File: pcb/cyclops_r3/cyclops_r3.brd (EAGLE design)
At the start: 69.8 x 53.3 mm, 111 parts, among them M12_TUBE_MOUNT PT-LH001, Q1 SUM11006, Q2 IRF540, U1 MCP4921, U10 AD829, U11 MIC5225, U12 MIC5270, U2 317-N, U3 TLV37, U4 337-N, U5 ADR03, U6 OP1177, U7 TLV2374, U8 ZXTD45, U9 ADA4899

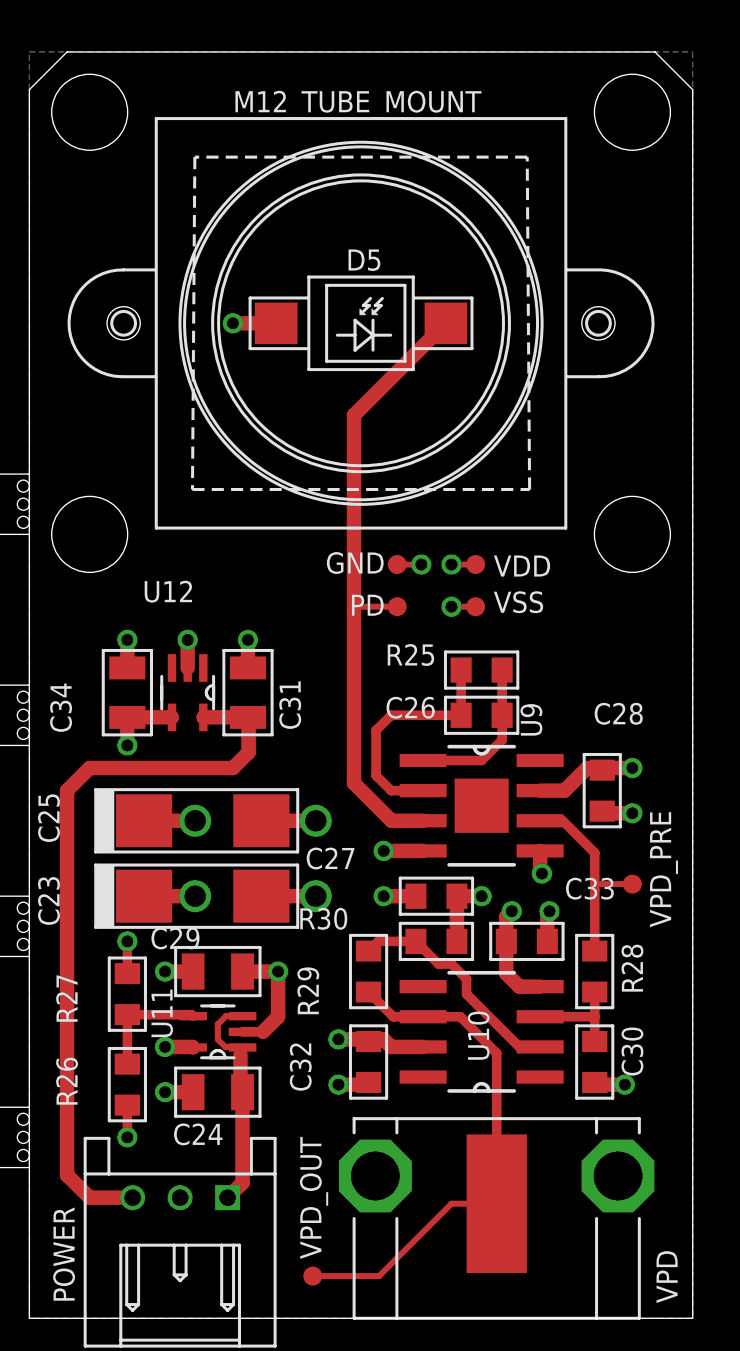
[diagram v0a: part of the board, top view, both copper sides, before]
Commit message: Added a compensation cap and offset null pot to the PD circuit.
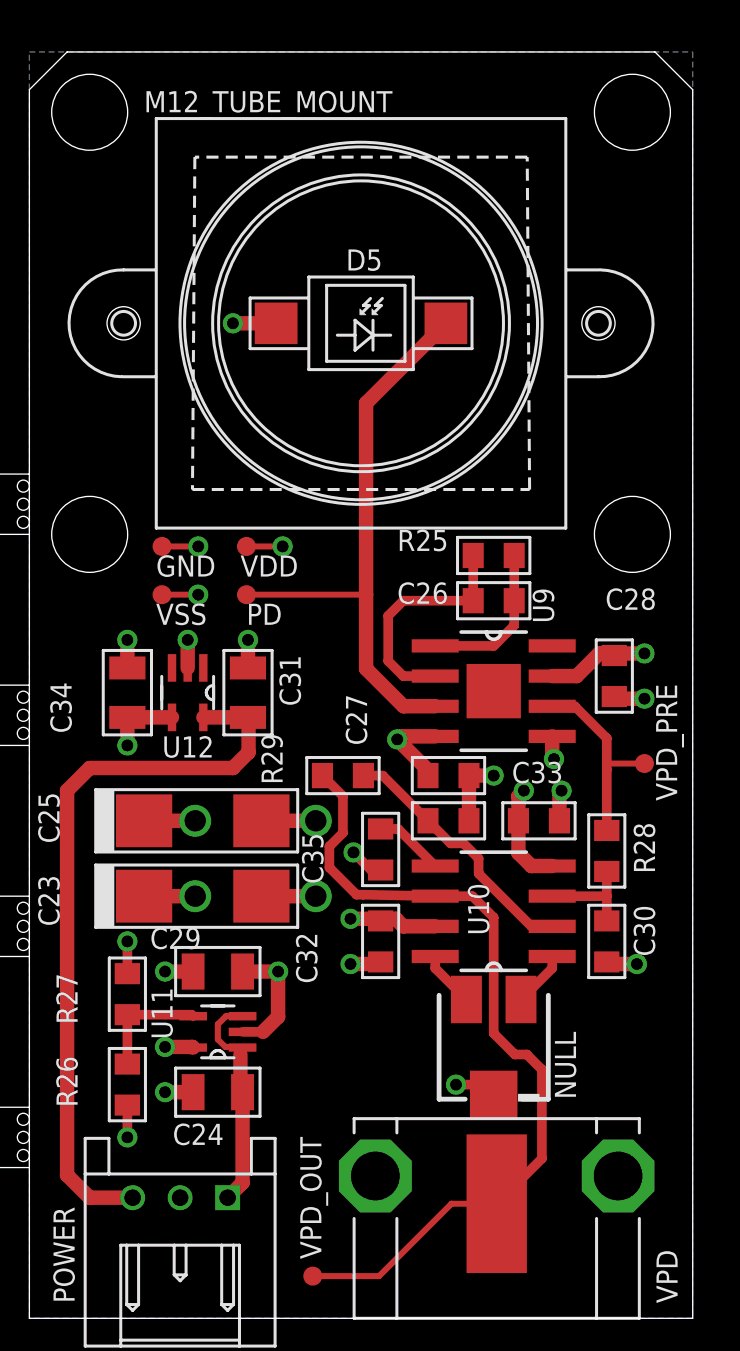
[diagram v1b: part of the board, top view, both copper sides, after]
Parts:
- added C35: 10pF, cyclops:0603
- added NULL: 20k, cyclops:SM-42/43A
- moved VSS 13.2 mm to (76.7, 30.5)
- moved GND 9.94 mm to (76.7, 32.5)
- moved VDD 9.68 mm to (80.3, 32.5)
- moved R29 8.33 mm to (84.3, 22.9), turned to 0 degrees
- moved PD 6.37 mm to (80.3, 30.5)
- moved C30 5.11 mm to (95.4, 15.9)
- moved C32 5.11 mm to (85.9, 15.9)
- moved U10 5.11 mm to (90.7, 17.1)
- moved VPD_PRE 5.11 mm to (97.0, 23.4)
- moved C27 5.11 mm to (88.8, 22.9)
- moved C33 5.11 mm to (92.6, 21.0)
- moved R28 5.11 mm to (95.4, 19.7)
- moved R30 5.11 mm to (88.8, 21.0)
- moved C26 4.85 mm to (90.7, 30.2)
- moved R25 4.85 mm to (90.7, 32.1)
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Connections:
- new net N$18: NULL.3, U10.1
- new net N$25: NULL.1, U10.8
- new net N$26: C35.1, U10.5
- net -5V: now also NULL.2
- net AGND: now also C35.2
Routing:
- net VPD: track 21.8 -> 35.2 mm
- net -5V: track 16.6 -> 19.5 mm
- net N$26: track 0.00 -> 2.95 mm
- net N$25: track 0.00 -> 2.35 mm
- net N$18: track 0.00 -> 2.35 mm
- net AGND: track 24.9 -> 26.8 mm, vias 14 -> 15
- net N$19: track 26.4 -> 24.5 mm
- net N$24: track 9.61 -> 11.0 mm
- net +7V: track 15.0 -> 15.5 mm

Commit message: Minor.
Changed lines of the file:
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@@
 <layer number="27" name="tValues" color="7" fill="1" visible="yes" active="yes"/>
 <layer number="28" name="bValues" color="7" fill="1" visible="yes" active="yes"/>
-<layer number="29" name="tStop" color="7" fill="3" visible="yes" active="yes"/>
+<layer number="29" name="tStop" color="7" fill="3" visible="no" active="yes"/>
 <layer number="30" name="bStop" color="7" fill="6" visible="no" active="yes"/>
 <layer number="31" name="tCream" color="7" fill="4" visible="no" active="yes"/>
@@
 <contactref element="VPD" pad="1"/>
 <wire x1="90.805" y1="4.826" x2="92.71" y2="6.731" width="0.4064" layer="1"/>
-<wire x1="92.71" y1="6.731" x2="93.726" y2="7.747" width="0" layer="19" extent="1-16"/>
 <wire x1="89.779975" y1="17.78" x2="88.2142" y2="17.78" width="0.4064" layer="1"/>
 <wire x1="85.1789" y1="17.8435" x2="88.2142" y2="17.78" width="0.4064" layer="1"/>
@@
 <wire x1="83.7565" y1="19.8755" x2="84.328" y2="20.447" width="0.4064" layer="1"/>
 <wire x1="89.779975" y1="17.78" x2="90.678" y2="16.881975" width="0.4064" layer="1"/>
-<wire x1="90.678" y1="16.881975" x2="90.678" y2="12.0015" width="0.4064" layer="1"/>
-<wire x1="90.678" y1="12.0015" x2="91.567" y2="11.1125" width="0.4064" layer="1"/>
-<wire x1="91.567" y1="11.1125" x2="92.075" y2="11.1125" width="0.4064" layer="1"/>
-<wire x1="92.075" y1="11.1125" x2="92.71" y2="10.4775" width="0.4064" layer="1"/>
-<wire x1="92.71" y1="10.4775" x2="92.71" y2="6.731" width="0.4064" layer="1"/>
+<wire x1="90.678" y1="16.881975" x2="90.678" y2="12.1285" width="0.4064" layer="1"/>
+<wire x1="92.71" y1="10.0965" x2="92.71" y2="6.731" width="0.4064" layer="1"/>
+<wire x1="90.678" y1="12.1285" x2="92.71" y2="10.0965" width="0.4064" layer="1"/>
 </signal>
 <signal name="N$23">

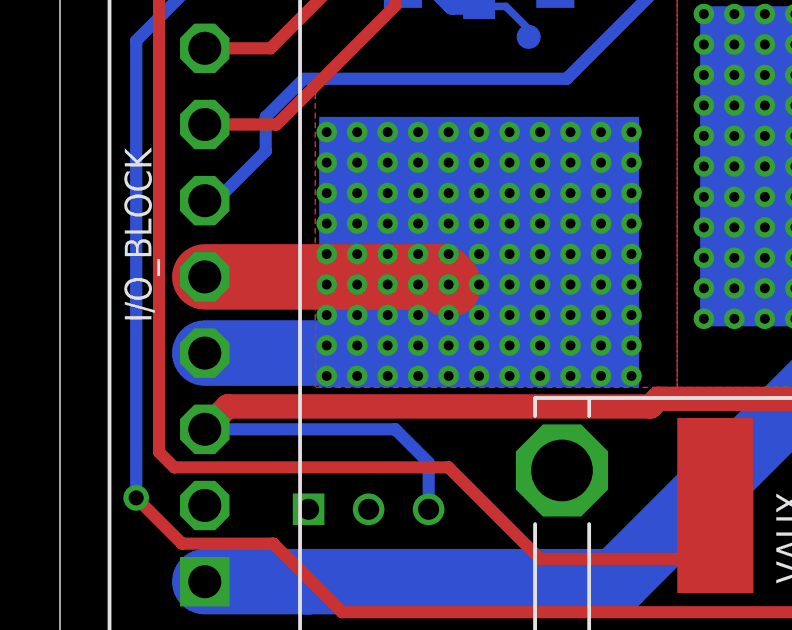
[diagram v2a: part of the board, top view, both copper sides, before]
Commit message: Started fixing and documenting problems form the first r3.0 build.
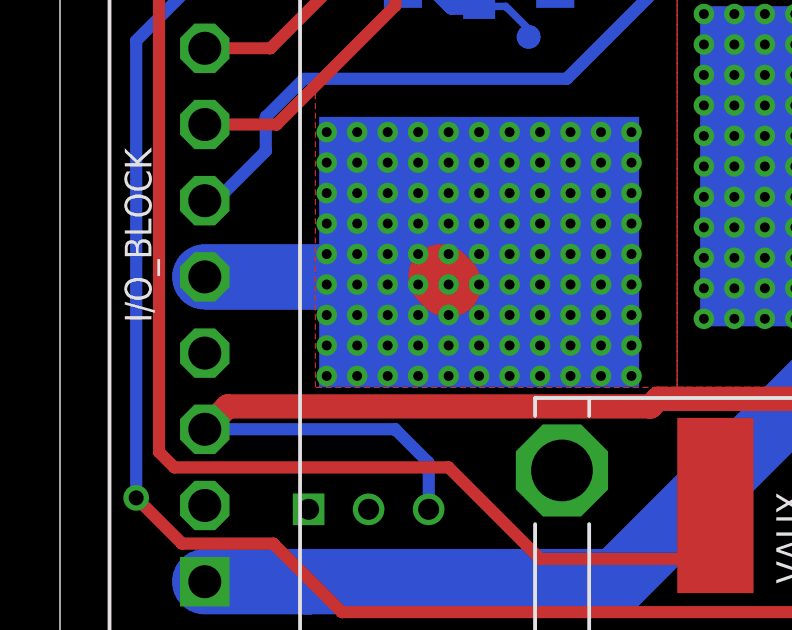
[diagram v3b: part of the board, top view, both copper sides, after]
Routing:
- net +12V: track 77.2 -> 68.1 mm
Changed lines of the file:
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@@
 <wire x1="55.753" y1="22.479" x2="56.6674" y2="22.479" width="0.4064" layer="16"/>
 <contactref element="I/O_BLOCK" pad="P$4"/>
-<wire x1="3.556" y1="9.906" x2="12.7" y2="9.906" width="2.1844" layer="16"/>
 <wire x1="12.7" y1="9.906" x2="12.7" y2="15.24" width="2.1844" layer="16"/>
 <wire x1="46.7614" y1="20.574" x2="46.736" y2="20.574" width="0.4064" layer="1"/>
@@
 <wire x1="56.6674" y1="22.479" x2="79.0575" y2="12.3825" width="0" layer="19" extent="1-16"/>
 <wire x1="33.9852" y1="28.8925" x2="27.305" y2="28.829" width="0" layer="19" extent="16-16"/>
+<wire x1="12.7" y1="9.906" x2="7.017" y2="4.699" width="0" layer="19" extent="16-16"/>
 </signal>
 <signal name="N$72">
@@
 <contactref element="I/O_BLOCK" pad="P$5"/>
 <via x="12.7" y="15.24" extent="1-16" drill="0.3302"/>
-<wire x1="3.556" y1="12.446" x2="11.43" y2="12.446" width="2.1844" layer="1"/>
+<wire x1="3.556" y1="12.446" x2="11.43" y2="12.446" width="2.1844" layer="16"/>
 <wire x1="11.43" y1="12.446" x2="11.684" y2="12.192" width="2.1844" layer="1"/>
 <wire x1="12.7" y1="13.6525" x2="12.7" y2="13.208" width="0.4064" layer="16"/>
+<wire x1="11.43" y1="12.446" x2="11.43" y2="12.446" width="0" layer="19" extent="1-16"/>
 </signal>
 <signal name="REFA">

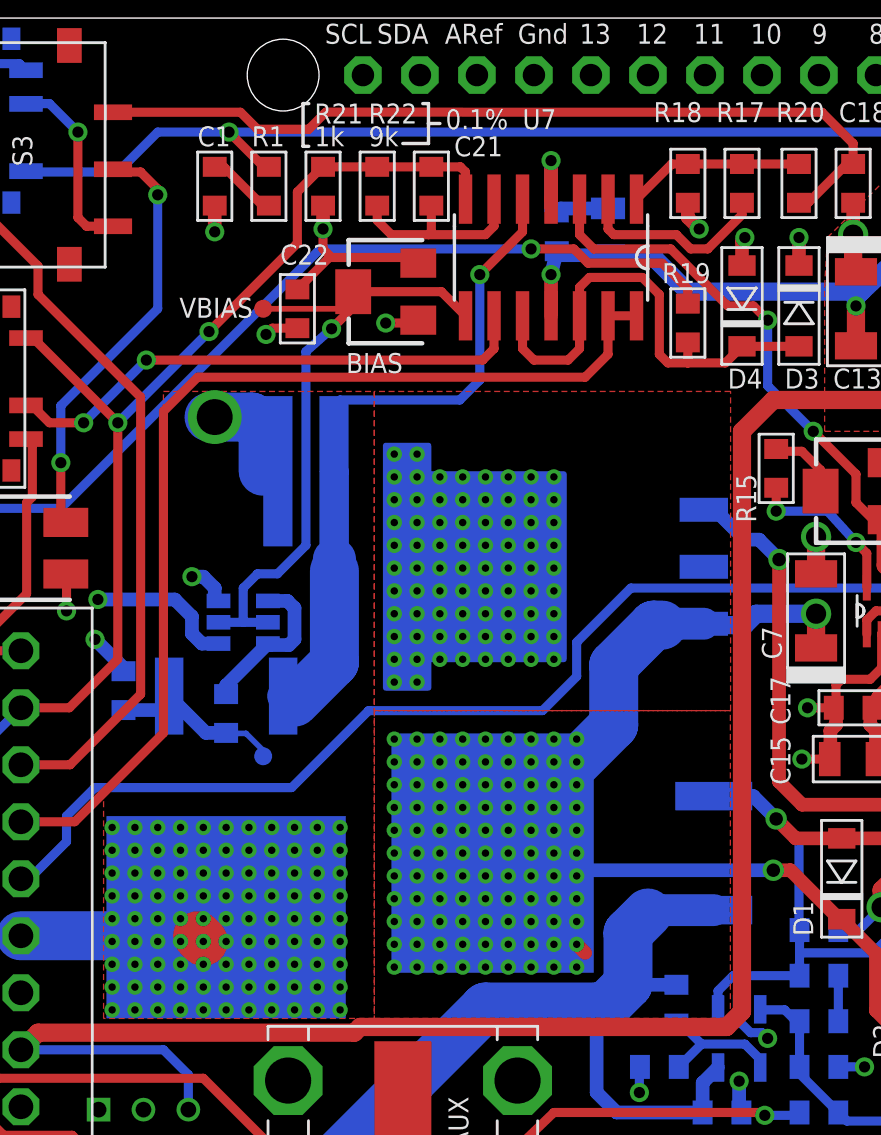
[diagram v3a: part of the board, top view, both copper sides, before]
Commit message: Fixed some wiring problems, added some notes.
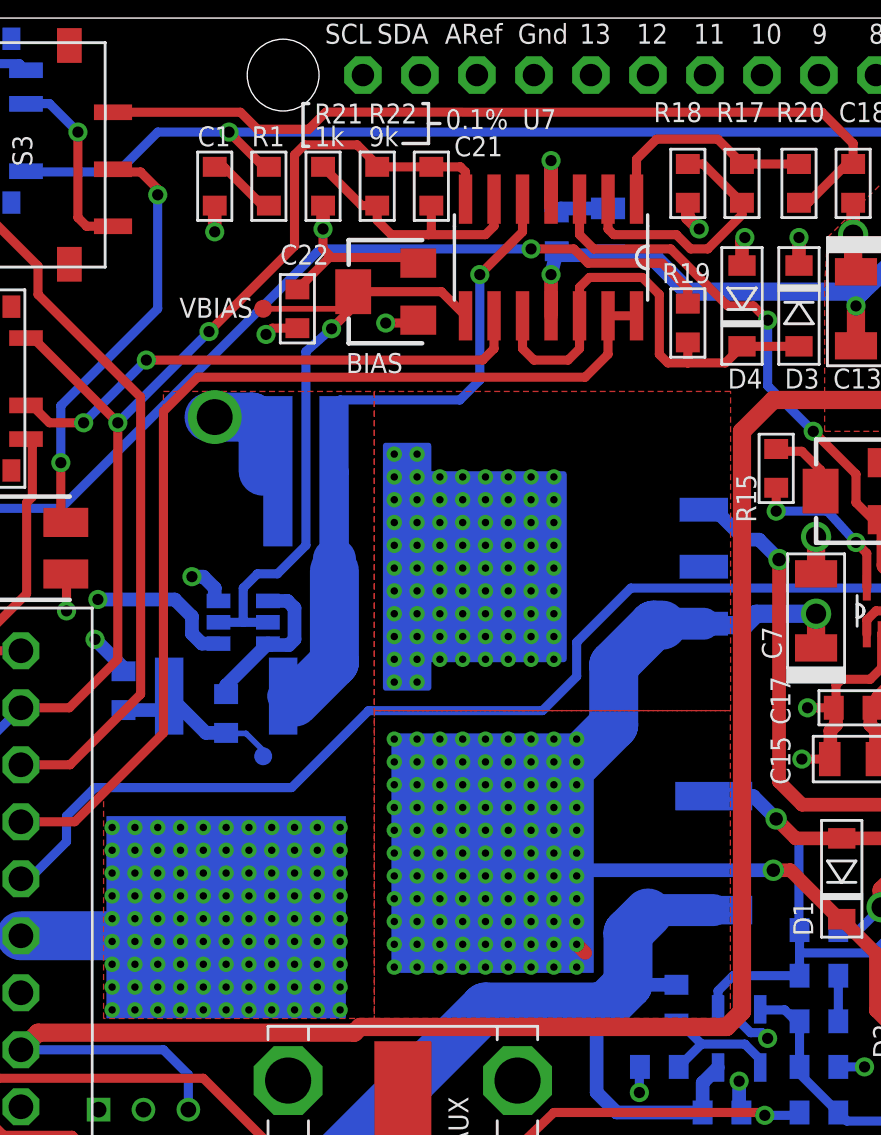
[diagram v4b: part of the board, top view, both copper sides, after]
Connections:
- net N$15: now also R21.1
- net N$8: now also R18.1
- net VI: no longer R21.1
- net VREFA2X: no longer R18.1
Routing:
- net LED-: track 12.9 -> 8.32 mm
- net N$8: track 8.83 -> 12.0 mm
- net N$15: track 8.84 -> 12.0 mm
- net VREFA2X: track 7.89 -> 9.86 mm
- net VI: track 102.8 -> 104.7 mm
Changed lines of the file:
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@@
 <wire x1="21.844" y1="44.9834" x2="21.844" y2="43.815" width="0.4064" layer="1"/>
 <wire x1="21.844" y1="43.815" x2="21.717" y2="43.688" width="0.4064" layer="1"/>
+<contactref element="R21" pad="1"/>
+<wire x1="19.431" y1="44.9834" x2="18.7452" y2="44.9834" width="0.4064" layer="1"/>
+<wire x1="18.7452" y1="44.9834" x2="17.018" y2="46.7106" width="0.4064" layer="1"/>
 </signal>
 <signal name="N$20">
@@
 <via x="9.652" y="16.256" extent="1-16" drill="0.3302"/>
 <contactref element="Q2" pad="D"/>
-<wire x1="9.7155" y1="10.668" x2="12.7" y2="13.6525" width="2.1844" layer="16"/>
 <contactref element="I/O_BLOCK" pad="P$5"/>
 <via x="12.7" y="15.24" extent="1-16" drill="0.3302"/>
 <wire x1="3.556" y1="12.446" x2="11.43" y2="12.446" width="2.1844" layer="16"/>
-<wire x1="11.43" y1="12.446" x2="11.684" y2="12.192" width="2.1844" layer="1"/>
 <wire x1="12.7" y1="13.6525" x2="12.7" y2="13.208" width="0.4064" layer="16"/>
-<wire x1="11.43" y1="12.446" x2="11.43" y2="12.446" width="0" layer="19" extent="1-16"/>
+<wire x1="11.684" y1="12.192" x2="11.43" y2="12.446" width="0" layer="19" extent="16-16"/>
 </signal>
 <signal name="REFA">
@@
 <contactref element="U7" pad="7"/>
 <contactref element="R22" pad="2"/>
-<contactref element="R21" pad="1"/>
 <contactref element="S5" pad="1"/>
 <wire x1="7.874" y1="24.765" x2="7.874" y2="35.306" width="0.4064" layer="1"/>
@@
 <wire x1="11.938" y1="39.37" x2="7.874" y2="35.306" width="0.4064" layer="16"/>
 <via x="7.874" y="35.306" extent="1-16" drill="0.5"/>
-<wire x1="17.018" y1="46.7106" x2="19.431" y2="46.7106" width="0.4064" layer="1"/>
-<wire x1="15.875" y1="45.593" x2="16.9926" y2="46.7106" width="0.4064" layer="1"/>
-<wire x1="16.9926" y1="46.7106" x2="17.018" y2="46.7106" width="0.4064" layer="1"/>
 <contactref element="R2" pad="2"/>
 <wire x1="1.27" y1="20.32" x2="1.27" y2="5.08" width="0.4064" layer="16"/>
@@
 <wire x1="23.1394" y1="46.7106" x2="23.368" y2="46.482" width="0.4064" layer="1"/>
 <wire x1="23.368" y1="46.482" x2="23.368" y2="45.272" width="0.4064" layer="1"/>
-<wire x1="11.938" y1="39.37" x2="15.875" y2="43.307" width="0.4064" layer="1"/>
-<wire x1="15.875" y1="43.307" x2="15.875" y2="45.593" width="0.4064" layer="1"/>
+<wire x1="11.938" y1="39.37" x2="15.748" y2="43.18" width="0.4064" layer="1"/>
 <contactref element="I/O_BLOCK" pad="P$9"/>
 <wire x1="3.556" y1="22.606" x2="5.715" y2="22.606" width="0.4064" layer="1"/>
 <wire x1="5.715" y1="22.606" x2="7.874" y2="24.765" width="0.4064" layer="1"/>
 <wire x1="1.27" y1="20.32" x2="3.556" y2="22.606" width="0.4064" layer="16"/>
+<wire x1="19.431" y1="46.7106" x2="19.431" y2="46.7995" width="0.4064" layer="1"/>
+<wire x1="19.431" y1="46.7995" x2="18.542" y2="47.6885" width="0.4064" layer="1"/>
+<wire x1="18.542" y1="47.6885" x2="16.1925" y2="47.6885" width="0.4064" layer="1"/>
+<wire x1="16.1925" y1="47.6885" x2="15.748" y2="47.244" width="0.4064" layer="1"/>
+<wire x1="15.748" y1="47.244" x2="15.748" y2="43.18" width="0.4064" layer="1"/>
 </signal>
 <signal name="N$7">
@@
 <contactref element="U7" pad="1"/>
 <contactref element="R17" pad="1"/>
-<contactref element="R18" pad="1"/>
 <contactref element="R20" pad="1"/>
-<wire x1="30.988" y1="45.272" x2="32.5536" y2="46.8376" width="0.4064" layer="1"/>
-<wire x1="32.5536" y1="46.8376" x2="33.274" y2="46.8376" width="0.4064" layer="1"/>
 <wire x1="35.687" y1="46.8376" x2="38.227" y2="46.8376" width="0.4064" layer="1"/>
-<wire x1="33.274" y1="46.8376" x2="35.687" y2="46.8376" width="0.4064" layer="1"/>
+<wire x1="35.687" y1="46.8376" x2="35.687" y2="46.863" width="0.4064" layer="1"/>
+<wire x1="35.687" y1="46.863" x2="34.6075" y2="47.9425" width="0.4064" layer="1"/>
+<wire x1="34.6075" y1="47.9425" x2="31.877" y2="47.9425" width="0.4064" layer="1"/>
+<wire x1="31.877" y1="47.9425" x2="30.988" y2="47.0535" width="0.4064" layer="1"/>
+<wire x1="30.988" y1="47.0535" x2="30.988" y2="45.272" width="0.4064" layer="1"/>
 </signal>
 <signal name="N$8">
@@
 <wire x1="35.687" y1="44.577" x2="35.687" y2="45.085" width="0.4064" layer="1"/>
 <wire x1="35.687" y1="45.085" x2="35.687" y2="45.1104" width="0.6096" layer="1"/>
+<contactref element="R18" pad="1"/>
+<wire x1="33.274" y1="46.8376" x2="33.9598" y2="46.8376" width="0.4064" layer="1"/>
+<wire x1="33.9598" y1="46.8376" x2="35.687" y2="45.1104" width="0.4064" layer="1"/>
 </signal>
 <signal name="N$4">
